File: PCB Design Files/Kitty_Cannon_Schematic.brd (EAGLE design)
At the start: 66 x 100.3 mm, 11 parts, among them J1 DCJ200-10-A-XX-X_REVA, J2 RASPBERRYPI-40-PIN-GPIO_PTH, J3 DCJ200-10-A-XX-X_REVA, J4 DCJ200-10-A-XX-X_REVA, J5 USB1040-XX-X-X_REVC, U1 LD1085V50

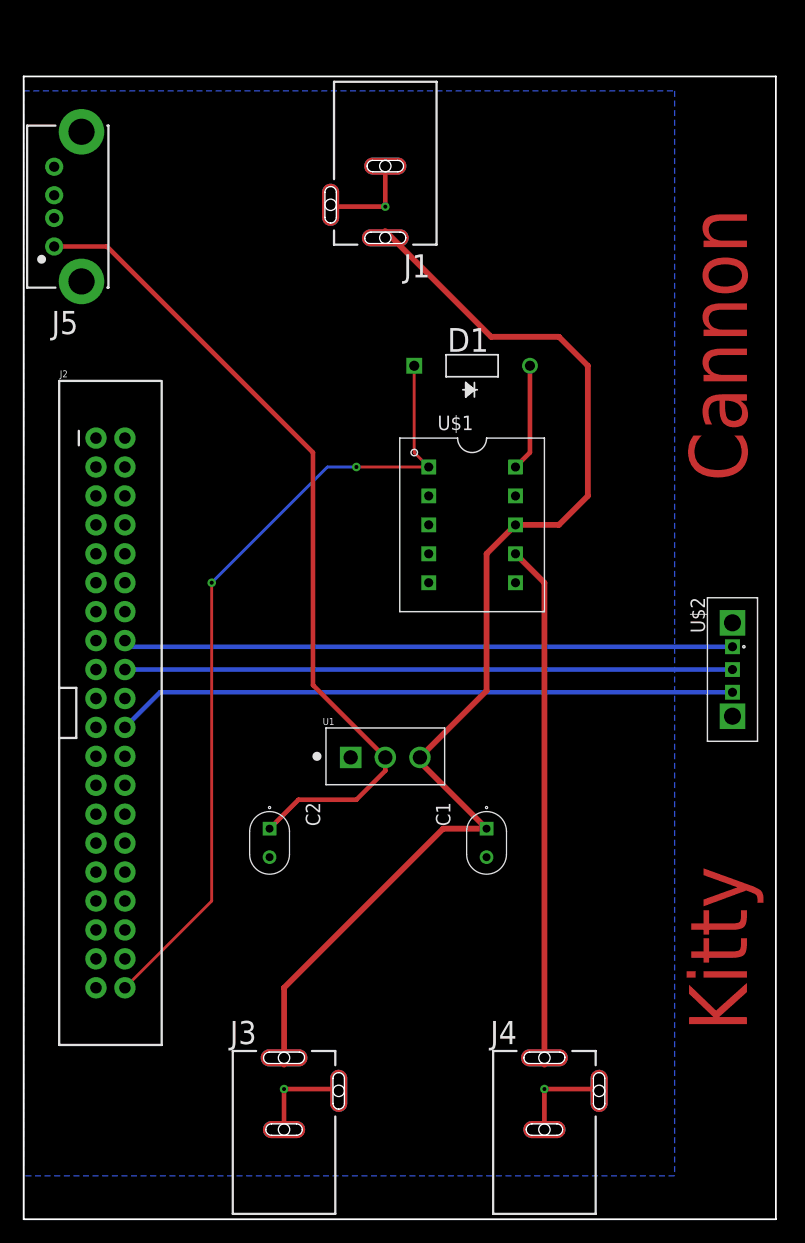
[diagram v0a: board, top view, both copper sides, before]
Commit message: Kitty Cannon - update structure
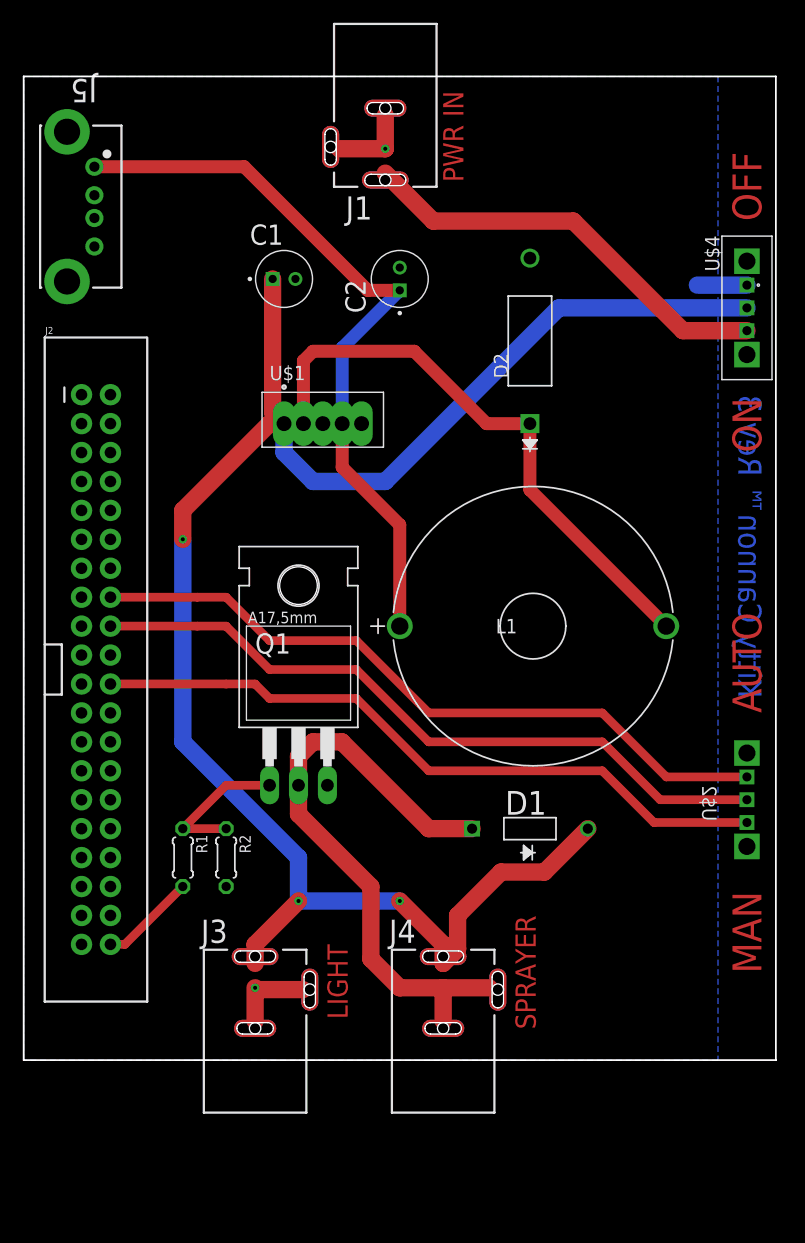
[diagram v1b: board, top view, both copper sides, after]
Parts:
- removed U1: LD1085V50, LD1085V50:TO-220-3
- added D2: SB3100E-G, SB3100E-G_Schottky:SB2E-G
- added L1: 330uH, 1433428C_330uH:1433428C_MUR
- added Q1: TIP120, transistor-power:TO220AH
- added R1: 270, rcl:0204/5
- added R2: 10k, rcl:0204/5
- added U$4: OS102011MA1QN1, C&K:OS102011MA1QN1
- C1: value FK16X7R1C106KR006 -> 100uF; device FK16X7R1C106KR006:FK16 -> 860010372006_100uF:860010372006_100UF
- C2: value FK16X7R1C106KR006 -> 330uF; device FK16X7R1C106KR006:FK16 -> 860010372006_100uF:860010372006_100UF
- U$1: value EA2-3NJ -> LM2575-5.0WT; device Kemet:EA2-3NJ -> LM2575-5.0WT:LM2575-5.0WT
- moved C1 51.4 mm to (22.9, 82.5), turned to 0 degrees
- moved C2 49.6 mm to (33.0, 82.5), turned to 90 degrees
- moved D1 41.0 mm to (39.4, 34.3)
- moved U$1 20.7 mm to (29.2, 68.6)
- moved J4 12.6 mm to (36.8, 16.5)
- moved U$2 11.5 mm to (63.5, 36.8), flipped to the bottom
- moved J3 9.25 mm to (20.3, 16.5)
- moved J1 5.08 mm to (31.8, 97.8)
- moved J2 4.02 mm to (6.35, 48.3)
- moved J5 1.27 mm to (3.81, 88.9), turned to 270 degrees
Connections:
- net N$1 renamed MAN
- net N$2 renamed AUTO
- net N$7 renamed CONN
- removed net 12V_EN: J4.1, U$1.7
- removed net 3.3V: J2.1, J2.17
- removed net 5V: J2.2, J2.4
- new net 3V3_BASE: Q1.B, R1.1, R2.1
- new net N$1: J2.2
- new net N$2: J2.4
- new net N$3: J2.1
- new net N$4: J2.17
- new net ON: J1.1, U$4.3
- new net REG_OUT: D2.1, L1.2, U$1.2
- new net SPRAY_RET: D1.2, J4.2, J4.3, Q1.C
- net 12V: now also D1.1, J4.1, U$1.1, U$4.2; no longer J1.1, U$1.8, U1.3
- net 3V3_EN: now also R1.2; no longer D1.2, U$1.1
- net 5V_IN: now also L1.1, U$1.4; no longer U1.2
- net GND: now also D2.2, Q1.E, R2.2, U$1.3, U$1.5, U$4.1; no longer D1.1, J4.2, J4.3, U$1.10, U1.1
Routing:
- net 3V3_EN: track 71.4 -> 8.45 mm, vias 2 -> 0
- net SPRAY_RET: track 0.00 -> 53.9 mm
- net 12V: track 104.4 -> 156.5 mm, vias 0 -> 3
- net REG_OUT: track 0.00 -> 51.1 mm
- net 12V_EN: track 45.9 -> 0.00 mm
- net ON: track 0.00 -> 37.5 mm
- net 3V3_BASE: track 0.00 -> 13.0 mm
- net GND: track 30.9 -> 18.7 mm, vias 3 -> 2
- net CONN: track 53.3 -> 62.2 mm
- net AUTO: track 53.6 -> 62.4 mm
- net 5V_IN: track 73.0 -> 65.0 mm
- net MAN: track 54.6 -> 60.9 mm
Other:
- board size 66 x 100.3 mm -> 66 x 86.4 mm
- board text added: "AUTO"
- board text added: "Kitty Cannon™ Rev 3"
- board text added: "LIGHT"
- board text added: "MAN"
- board text added: "OFF"
- board text added: "ON"
- board text added: "PWR IN"
- board text added: "SPRAYER"
- board text removed: "Cannon"
- board text removed: "Kitty"
